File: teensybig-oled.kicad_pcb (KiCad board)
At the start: 2 copper layers, 40.4 x 55.1 mm, 10 parts, among them J1 TEENSY-LC, J2 OLED_128x64

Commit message: slim version
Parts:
- removed the G*** at (88.3, 118.1)
- removed the G*** at (91.4, 94.7)
- removed the REF** at (103.0, 82.4)
- removed the REF** at (74.0, 81.9)
- removed the REF** at (103.1, 122.8)
- removed the REF** at (99.2, 97.9)
- removed the REF** at (84.3, 100.1)
- removed the REF** at (105.8, 124.2)
- added G***: LOGO, teensy-big-oled:osh-park-logo-300dpi-normal-copper, F.Cu at (145.9, 99.7)
- added G***: LOGO, teensy-big-oled:osh-park-logo-300dpi-normal-silk, F.Cu at (146.2, 119.0)
- added G***: LOGO, teensy-big-oled:osh-park-logo-300dpi-normal-silk, F.Cu at (161.9, 127.4)
- added REF**: Symbol_OSHW-Logo_SilkScreen, Wickerlib:Symbol_OSHW-Logo_SilkScreen, B.Cu at (146.1, 103.5)
- added REF**: Symbol_OSHW-Logo_SilkScreen, Wickerlib:Symbol_OSHW-Logo_SilkScreen, F.Cu at (162.1, 125.9)
- moved J1 63.3 mm to (148.5, 105.0)
- moved J2 59.5 mm to (162.7, 101.9)
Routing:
- net (no net): track 50.7 -> 0.00 mm
- net /DC: track 67.5 -> 28.9 mm
- net /CLK: track 50.7 -> 26.8 mm, vias 4 -> 1
- net /CS: track 52.9 -> 32.1 mm, vias 2 -> 1
- net /Data: track 45.6 -> 25.2 mm, vias 1 -> 0
- net /VIN: track 14.6 -> 0.00 mm
- net /RST: track 26.4 -> 19.9 mm, vias 2 -> 0
- added copper zone on B.Cu, net /VIN
- removed copper zone on B.Cu, net (none)
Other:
- board size 40.4 x 55.1 mm -> 32.6 x 41.2 mm
- net class Default: clearance 0.762 -> 0.1524; trace_width 0.3302 -> 0.254; via_dia 1.524 -> 0.762; via_drill 0.6858 -> 0.508
- rule trace_clearance: 0.762 -> 0.1524
- rule trace_min: 0.1524 -> 0.254
- rule via_min_drill: 0.3302 -> 0.508
- rule via_min_size: 0.6858 -> 0.762
- board text added: "DREW FUSTINI"
- board text removed: "Drew Fustini"

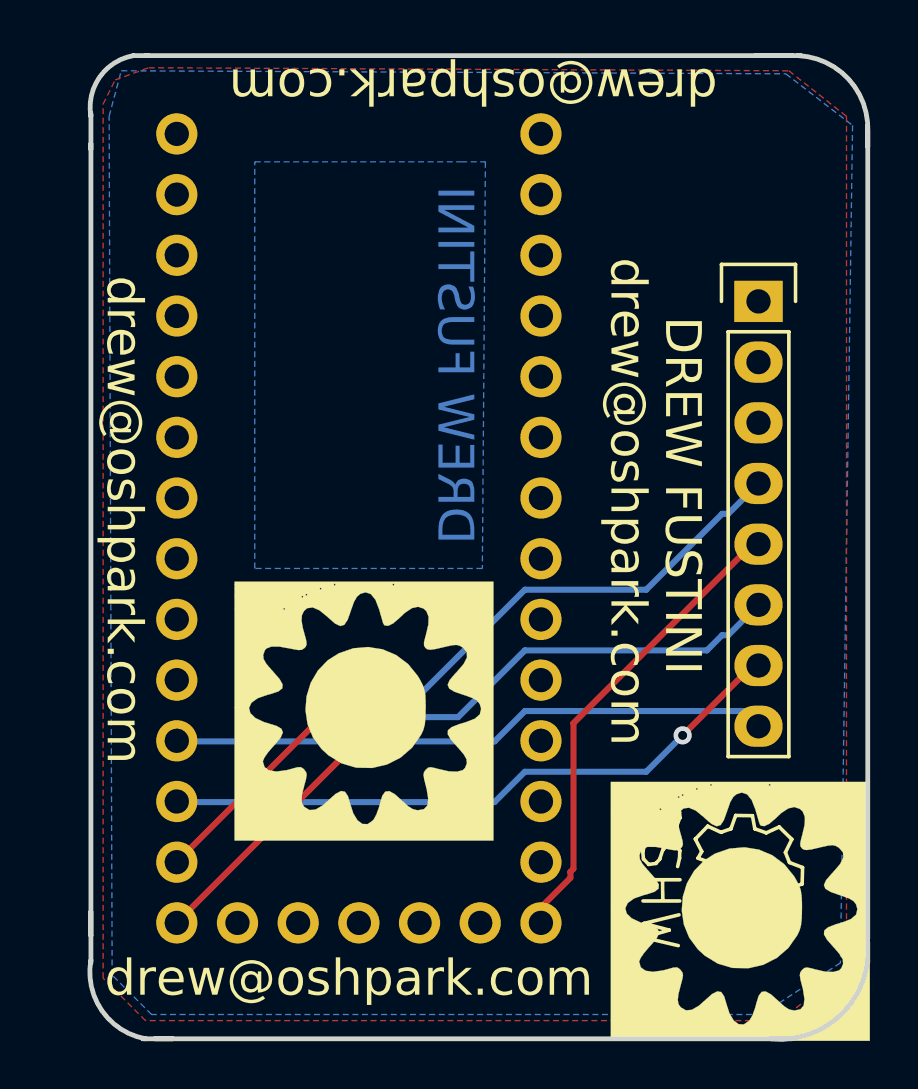
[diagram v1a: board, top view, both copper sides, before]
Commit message: fixed silkscreen logo, ordered slim version
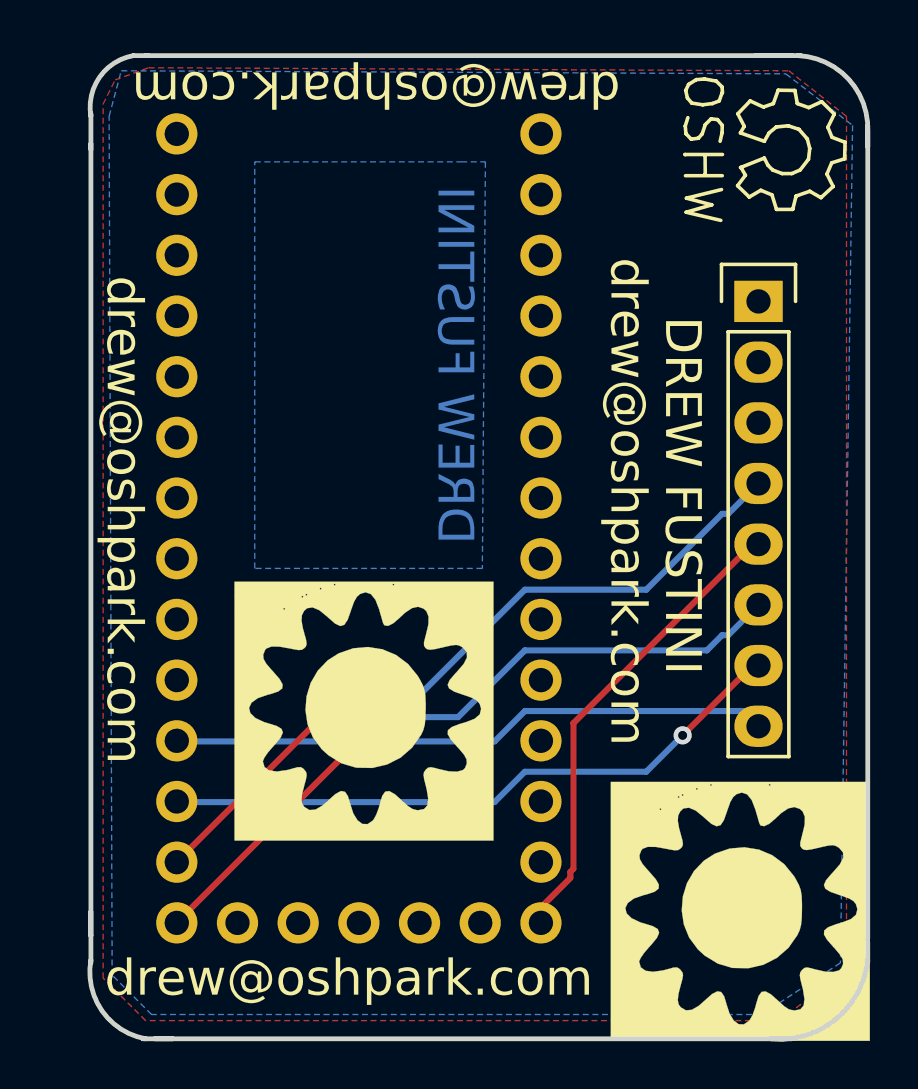
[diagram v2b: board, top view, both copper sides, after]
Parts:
- moved REF** 30.4 mm to (163.8, 95.5)
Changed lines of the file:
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@@
     (links 7)
     (no_connects 0)
-    (area 134.601193 91.466999 167.361646 132.834655)
+    (area 134.601193 91.134385 167.96202 138.227614)
     (thickness 1.6)
     (drawings 23)
@@
   )
   (module Wickerlib:Symbol_OSHW-Logo_SilkScreen (layer F.Cu)
-    (at 162.052 125.857 270)
+    (at 163.83 95.504 270)
     (descr "Symbol, OSHW-Logo, Silk Screen,")
     (tags "Symbol, OSHW-Logo, Silk Screen,")
@@
       (xy 0.172866 -2.680894) (xy 0.778728 -2.584594)) (layer F.SilkS) (width 0.01))
   )
-  (gr_text "drew@oshpark.com\n" (at 150.749 92.837 180) (layer F.SilkS)
+  (gr_text "drew@oshpark.com\n" (at 146.685 92.964 180) (layer F.SilkS)
     (effects (font (size 1.5 1.5) (thickness 0.3)))
   )

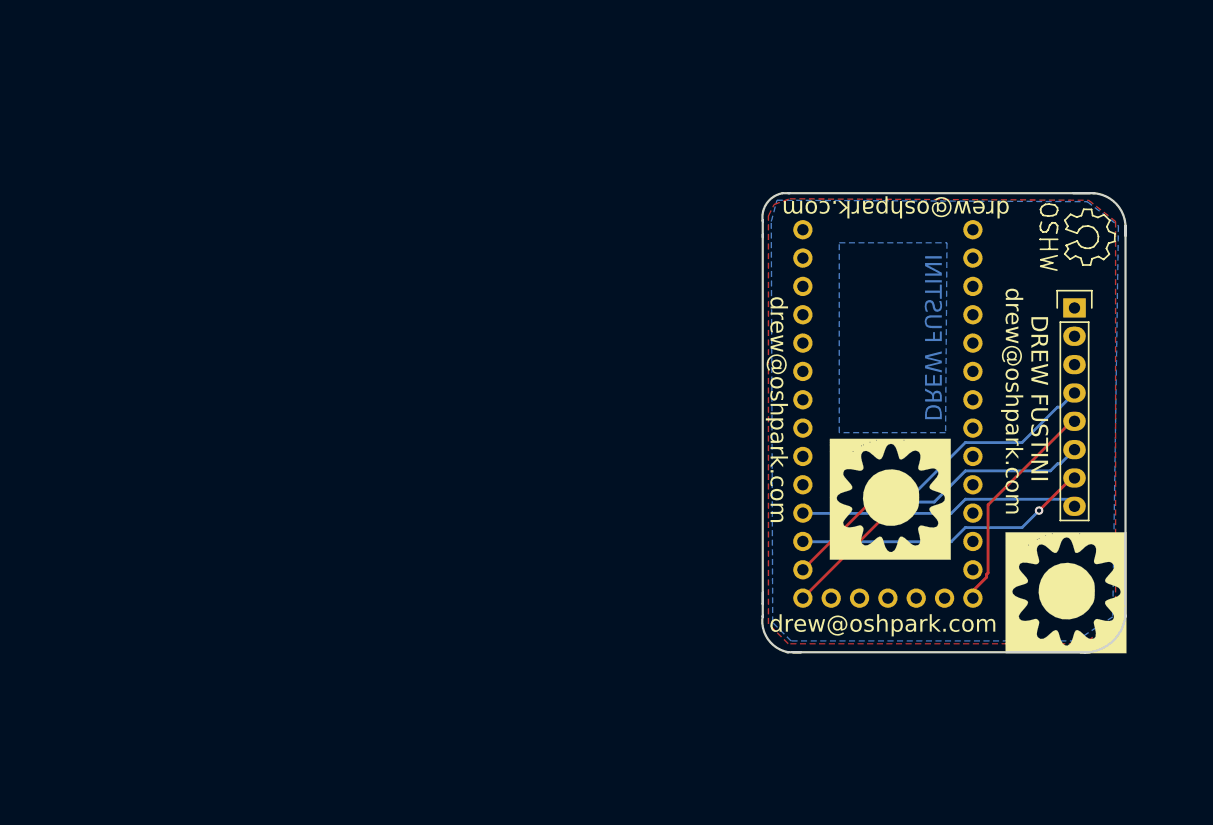
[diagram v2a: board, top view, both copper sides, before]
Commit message: add cap touch buttons
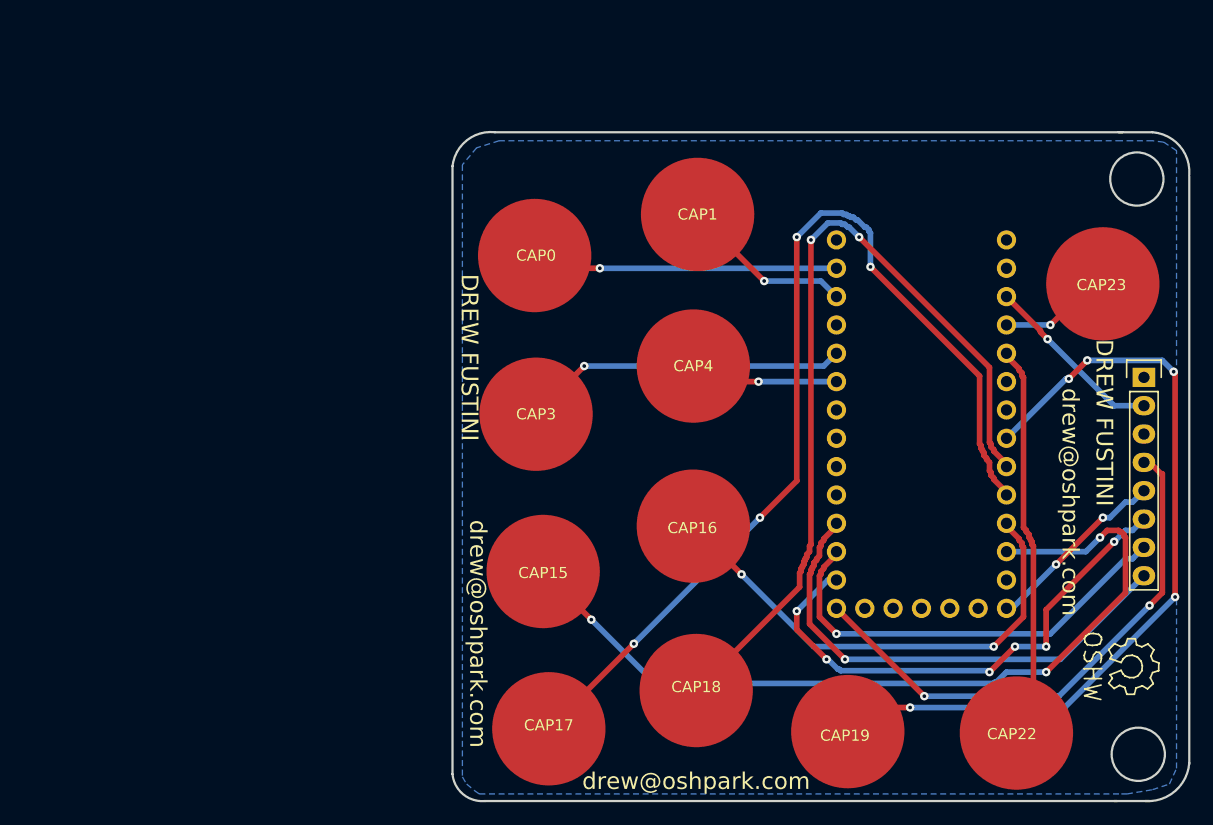
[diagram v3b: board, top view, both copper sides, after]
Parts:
- removed the G*** at (145.9, 99.7)
- removed the G*** at (146.2, 119.0)
- removed the G*** at (161.9, 127.4)
- removed the REF** at (146.1, 103.5)
- added CAP0: CAPSENSE_CIRCLE, Wickerlib:CAPSENSE_CIRCLE_D10, F.Cu at (114.3, 97.2)
- added CAP1: CAPSENSE_CIRCLE, Wickerlib:CAPSENSE_CIRCLE_D10, F.Cu at (128.9, 93.5)
- added CAP15: CAPSENSE_CIRCLE, Wickerlib:CAPSENSE_CIRCLE_D10, F.Cu at (115.1, 125.5)
- added CAP16: CAPSENSE_CIRCLE, Wickerlib:CAPSENSE_CIRCLE_D10, F.Cu at (128.5, 121.4)
- added CAP17: CAPSENSE_CIRCLE, Wickerlib:CAPSENSE_CIRCLE_D10, F.Cu at (115.6, 139.6)
- added CAP18: CAPSENSE_CIRCLE, Wickerlib:CAPSENSE_CIRCLE_D10, F.Cu at (128.8, 136.1)
- added CAP19: CAPSENSE_CIRCLE, Wickerlib:CAPSENSE_CIRCLE_D10, F.Cu at (142.4, 139.8)
- added CAP22: CAPSENSE_CIRCLE, Wickerlib:CAPSENSE_CIRCLE_D10, F.Cu at (157.5, 140.0)
- added CAP23: CAPSENSE_CIRCLE, Wickerlib:CAPSENSE_CIRCLE_D10, F.Cu at (165.2, 99.7)
- added CAP3: CAPSENSE_CIRCLE, Wickerlib:CAPSENSE_CIRCLE_D10, F.Cu at (114.4, 111.4)
- added CAP4: CAPSENSE_CIRCLE, Wickerlib:CAPSENSE_CIRCLE_D10, F.Cu at (128.5, 107.1)
- added G***: LOGO, teensy-big-oled:oshpark-silk-dpi72, B.Cu at (140.8, 117.0)
- moved REF** 38.7 mm to (167.8, 134.0)
- moved J2 8.80 mm to (168.9, 108.1)
- moved J1 3.15 mm to (151.5, 105.9)
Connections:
- J1 pad 15: Net-(J1-Pad15) -> /CAP15
- J1 pad 16: Net-(J1-Pad16) -> /CAP16
- J1 pad 17: Net-(J1-Pad17) -> /CAP17
- J1 pad 18: Net-(J1-Pad18) -> /CAP18
- J1 pad 19: Net-(J1-Pad19) -> /CAP19
- J1 pad 22: Net-(J1-Pad22) -> /CAP22
- J1 pad 23: Net-(J1-Pad23) -> /CAP23
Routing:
- net /CAP17: track 0.00 -> 90.1 mm, vias 0 -> 4
- net /CAP15: track 0.00 -> 76.5 mm, vias 0 -> 3
- net /CAP18: track 0.00 -> 76.2 mm, vias 0 -> 2
- net /CAP19: track 0.00 -> 72.9 mm, vias 0 -> 5
- net /CAP16: track 0.00 -> 44.2 mm, vias 0 -> 2
- net /CAP22: track 0.00 -> 35.7 mm
- net Net-(CAP3-Pad1): track 0.00 -> 29.2 mm, vias 0 -> 1
- net Net-(CAP0-Pad1): track 0.00 -> 27.5 mm, vias 0 -> 1
- net /Data: track 25.2 -> 44.4 mm, vias 0 -> 1
- net /DC: track 28.9 -> 46.7 mm, vias 1 -> 6
- net /CS: track 32.1 -> 49.1 mm, vias 1 -> 2
- net /VIN: track 0.00 -> 16.4 mm, vias 0 -> 1
- net Net-(CAP1-Pad1): track 0.00 -> 15.5 mm, vias 0 -> 1
- net Net-(CAP4-Pad1): track 0.00 -> 13.4 mm, vias 0 -> 1
- net /CLK: track 26.8 -> 39.4 mm
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- added copper zone on B.Cu, net /GND
- removed copper zone on F.Cu, net /GND
- removed copper zone on B.Cu, net /VIN
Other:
- board size 32.6 x 41.2 mm -> 66 x 60 mm
- net class Default: trace_width 0.254 -> 0.1524; via_dia 0.762 -> 0.6858; via_drill 0.508 -> 0.3302
- rule trace_min: 0.254 -> 0.1524
- rule via_min_drill: 0.508 -> 0.3302
- rule via_min_size: 0.762 -> 0.6858
